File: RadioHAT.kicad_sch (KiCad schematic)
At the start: 2 parts, among them J1 RPi_GPIO

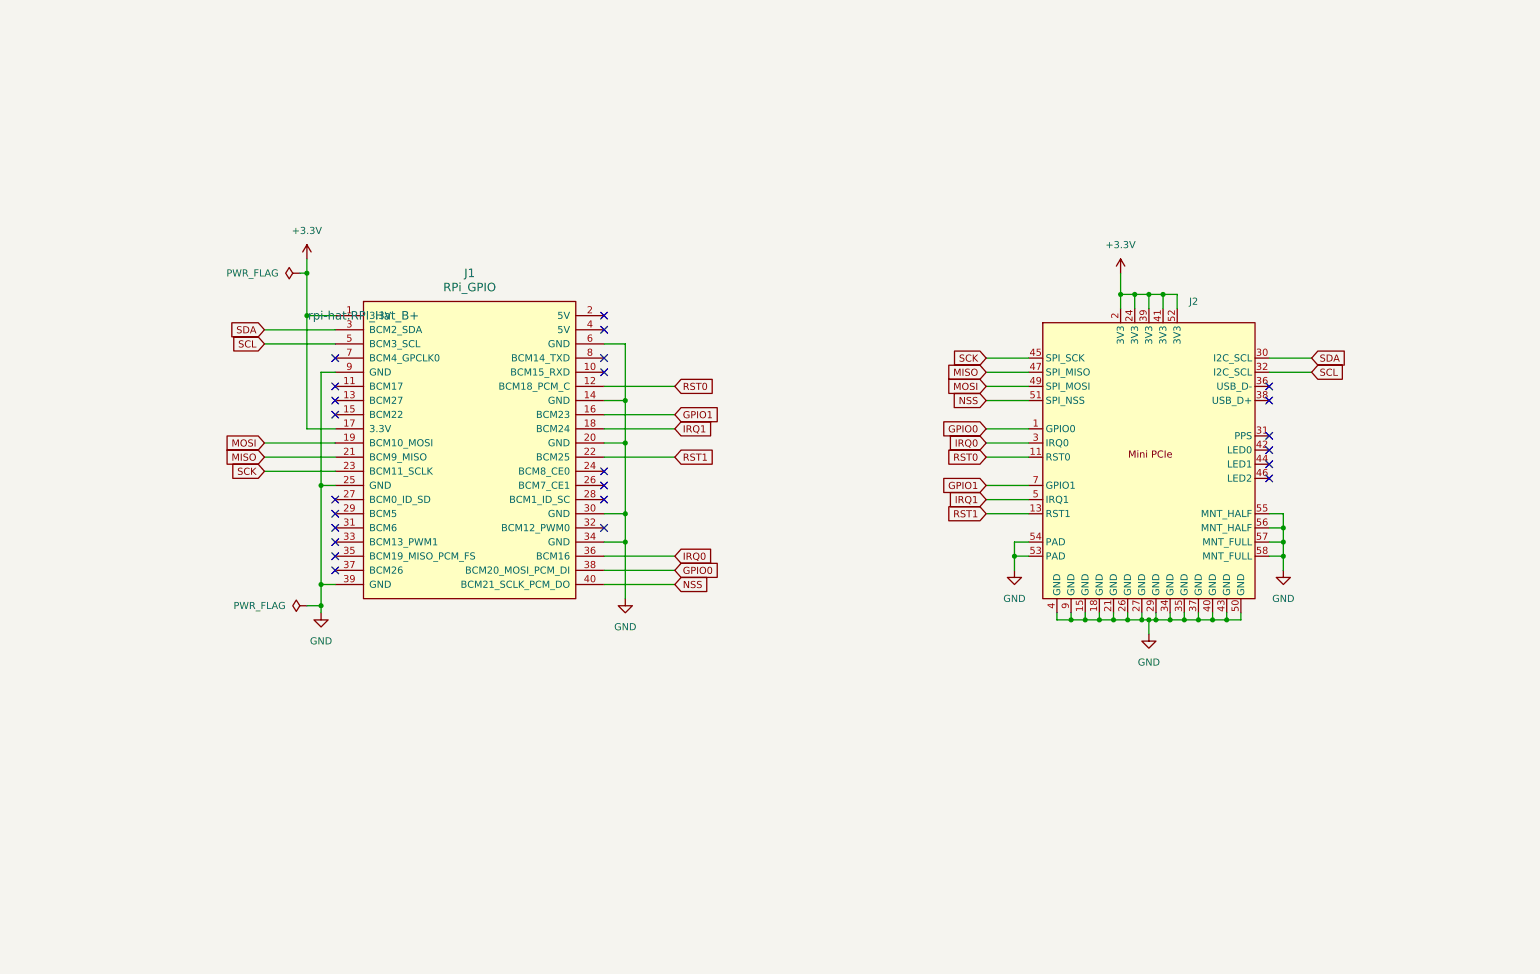
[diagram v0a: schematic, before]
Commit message: HAT rev C (GPIO sense, current measure, LDO)
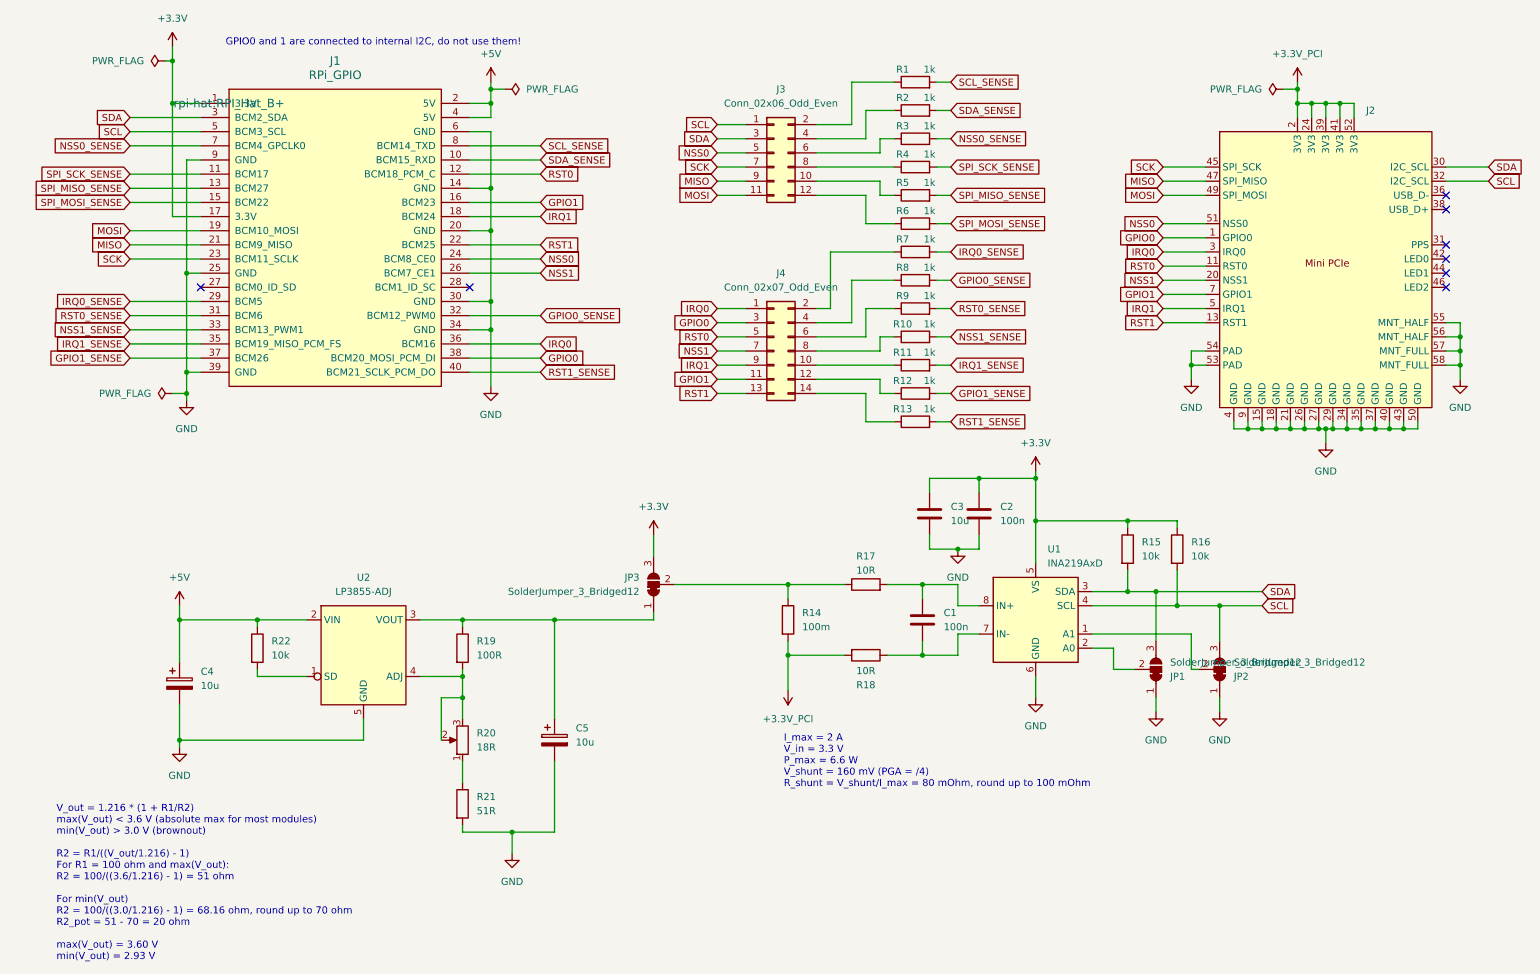
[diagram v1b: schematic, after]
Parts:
- added C1, C2: 100n, Capacitor_SMD:C_0603_1608Metric_Pad1.08x0.95mm_HandSolder, symbol Device:C
- added C3: 10u, Capacitor_SMD:C_0603_1608Metric_Pad1.08x0.95mm_HandSolder, symbol Device:C
- added C4, C5: 10u, Capacitor_Tantalum_SMD:CP_EIA-3216-18_Kemet-A, symbol Device:C_Polarized
- added J3: Conn_02x06_Odd_Even, Connector_PinHeader_2.54mm:PinHeader_2x06_P2.54mm_Vertical, symbol Connector_Generic:Conn_02x06_Odd_Even
- added J4: Conn_02x07_Odd_Even, Connector_PinHeader_2.54mm:PinHeader_2x07_P2.54mm_Vertical, symbol Connector_Generic:Conn_02x07_Odd_Even
- added JP1, JP2, JP3: SolderJumper_3_Bridged12, Jumper:SolderJumper-3_P1.3mm_Bridged12_Pad1.0x1.5mm_NumberLabels, symbol Jumper:SolderJumper_3_Bridged12
- added R1, R10, R11, R12, R13, R2, R3, R4, R5, R6, R7, R8, R9: 1k, Resistor_SMD:R_0805_2012Metric_Pad1.20x1.40mm_HandSolder, symbol Device:R
- added R14: 100m, Resistor_SMD:R_2816_7142Metric_Pad3.20x4.45mm_HandSolder, symbol Device:R
- added R15, R16, R22: 10k, Resistor_SMD:R_0603_1608Metric_Pad0.98x0.95mm_HandSolder, symbol Device:R
- added R17, R18: 10R, Resistor_SMD:R_0603_1608Metric_Pad0.98x0.95mm_HandSolder, symbol Device:R
- added R19: 100R, Resistor_SMD:R_0603_1608Metric_Pad0.98x0.95mm_HandSolder, symbol Device:R
- added R20: 18R, RadioHAT:3362P1200LF, symbol Device:R_Potentiometer
- added R21: 51R, Resistor_SMD:R_0603_1608Metric_Pad0.98x0.95mm_HandSolder, symbol Device:R
- added U1: INA219AxD, Package_SO:SOIC-8_3.9x4.9mm_P1.27mm, symbol Sensor_Energy:INA219AxD
- added U2: LP3855-ADJ, RadioHAT:SOT150P700X180-5N, symbol RadioHAT:LP3855-ADJ
- J2: footprint RadioHAT:Mini_PCIe -> RadioHAT:Mini_PCIe_Latch
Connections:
- net +3.3V: now also C2.1, C3.1, JP3.3 (B), R15.1, R16.1, U1.5 (VS); no longer J2.2 (3V3), J2.24 (3V3), J2.39 (3V3), J2.41 (3V3), J2.52 (3V3)
- net GND: now also C2.2, C3.2, C4.2, C5.2, JP1.1 (A), JP2.1 (A), R21.2, U1.6 (GND), U2.5 (GND)
- net GPIO0: now also J4.3 (Pin_3)
- net GPIO1: now also J4.11 (Pin_11)
- net IRQ0: now also J4.1 (Pin_1)
- net IRQ1: now also J4.9 (Pin_9)
- net MISO: now also J3.9 (Pin_9)
- net MOSI: now also J3.11 (Pin_11)
- net RST0: now also J4.5 (Pin_5)
- net RST1: now also J4.13 (Pin_13)
- net SCK: now also J3.7 (Pin_7)
- net SCL: now also J3.1 (Pin_1), JP2.3 (B), R16.2, U1.4 (SCL)
- net SDA: now also J3.3 (Pin_3), JP1.3 (B), R15.2, U1.3 (SDA)
- net SDA_SENSE: now reaches J1.10 (BCM15_RXD)
- net SDA_SENSE: now also R2.2
- net SPI_SCK_SENSE: now reaches J1.11 (BCM17)
- net SPI_SCK_SENSE: now also R4.2
- net SPI_MISO_SENSE: now reaches J1.13 (BCM27)
- net SPI_MISO_SENSE: now also R5.2
- net SPI_MOSI_SENSE: now reaches J1.15 (BCM22)
- net SPI_MOSI_SENSE: now also R6.2
- net +5V: now reaches J1.2 (5V)
- net +5V: now also J1.4 (5V), C4.1, R22.1, U2.2 (VIN)
- net NSS0: now reaches J1.24 (BCM8_CE0)
- net NSS0: now also J2.51 (NSS0), J3.5 (Pin_5)
- net NSS1: now reaches J1.26 (BCM7_CE1)
- net NSS1: now also J2.20 (NSS1), J4.7 (Pin_7)
- net IRQ0_SENSE: now reaches J1.29 (BCM5)
- net IRQ0_SENSE: now also R7.2
- net RST0_SENSE: now reaches J1.31 (BCM6)
- net RST0_SENSE: now also R9.2
- net GPIO0_SENSE: now reaches J1.32 (BCM12_PWM0)
- net GPIO0_SENSE: now also R8.2
- net NSS1_SENSE: now reaches J1.33 (BCM13_PWM1)
- net NSS1_SENSE: now also R10.2
- net IRQ1_SENSE: now reaches J1.35 (BCM19_MISO_PCM_FS)
- net IRQ1_SENSE: now also R11.2
- net GPIO1_SENSE: now reaches J1.37 (BCM26)
- net GPIO1_SENSE: now also R12.2
- net NSS0_SENSE: now reaches J1.7 (BCM4_GPCLK0)
- net NSS0_SENSE: now also R3.2
- net SCL_SENSE: now reaches J1.8 (BCM14_TXD)
- net SCL_SENSE: now also R1.2
- net NSS renamed RST1_SENSE
- net RST1_SENSE: now also R13.2; no longer J2.51 (SPI_NSS)
- new net: JP1.2 (C), U1.2 (A0)
- new net: J4.12 (Pin_12), R12.1
- new net: JP2.2 (C), U1.1 (A1)
- new net: JP3.2 (C), R14.1, R17.1
- new net: C1.1, R17.2, U1.8 (IN+)
- new net: J3.2 (Pin_2), R1.1
- new net: C1.2, R18.1, U1.7 (IN-)
- new net: J3.4 (Pin_4), R2.1
- new net: R22.2, U2.1 (SD)
- new net: C5.1, JP3.1 (A), R19.1, U2.3 (VOUT)
- new net: R19.2, R20.2, R20.3, U2.4 (ADJ)
- new net: J4.10 (Pin_10), R11.1
- new net: J3.10 (Pin_10), R5.1
- new net: J3.12 (Pin_12), R6.1
- new net: J4.14 (Pin_14), R13.1
- new net: J4.2 (Pin_2), R7.1
- new net: J4.4 (Pin_4), R8.1
- new net: J4.6 (Pin_6), R9.1
- new net: J4.8 (Pin_8), R10.1
- new net: R20.1, R21.1
- new net: J3.6 (Pin_6), R3.1
- new net: J3.8 (Pin_8), R4.1
- new net +3.3V_PCI: J2.2 (3V3), J2.24 (3V3), J2.39 (3V3), J2.41 (3V3), J2.52 (3V3), R14.2, R18.2
- no-connect marks 24 -> 8
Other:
- note added: "GPIO0 and 1 are connected to internal I2C, do not use them!"
- note added: "I_max = 2 A V_in = 3.3 V P_max = 6.6 W V_shunt = 160 mV (PGA = /4) R_shunt = V_shunt/I_max = 80 mOhm, round up to 100 mOhm"
- note added: "V_out = 1.216 * (1 + R1/R2) max(V_out) < 3.6 V (absolute max for most modules) min(V_out) > 3.0 V (brownout) R2 = R1/((V_out/1.216) - 1) For R1 = 100 ohm and max(V_out): R2 = 100/((3.6/1.216) - 1) = 51 ohm For min(V_out) R2 = 100/((3.0/1.216) - 1) = 68.16 ohm, round up to 70 ohm R2_pot = 51 - 70 = 20 ohm max(V_out) = 3.60 V min(V_out) = 2.93 V"
- moved on the sheet: J1

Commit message: Update to use new RPi HAT
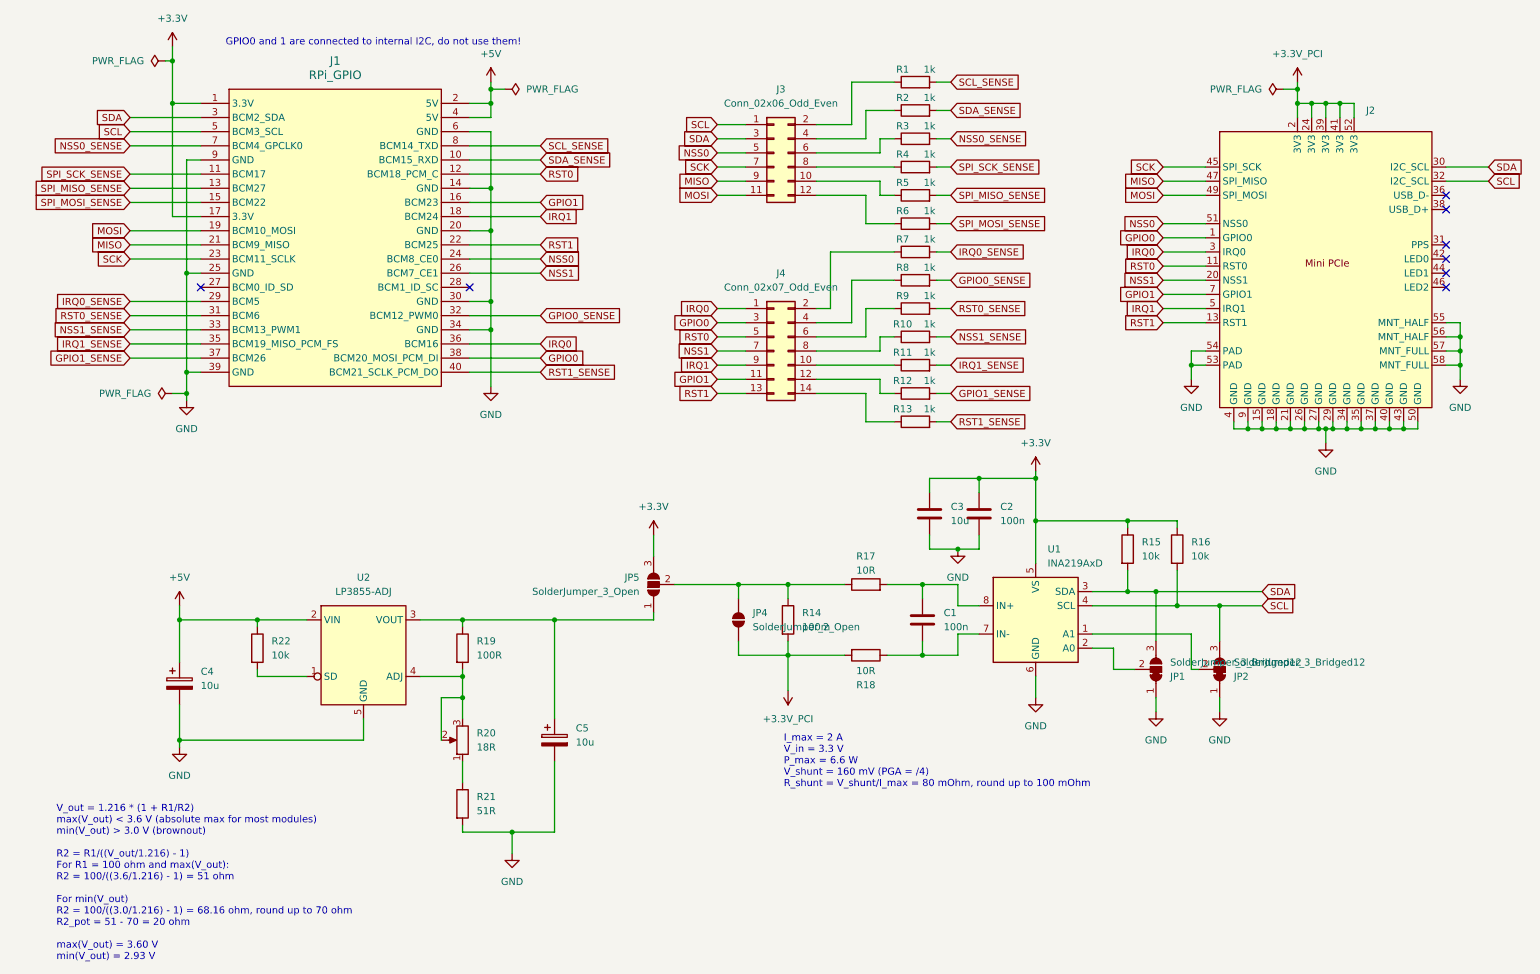
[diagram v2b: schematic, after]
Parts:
- removed JP3: SolderJumper_3_Bridged12, Jumper:SolderJumper-3_P1.3mm_Bridged12_Pad1.0x1.5mm_NumberLabels, symbol Jumper:SolderJumper_3_Bridged12
- added JP4: SolderJumper_2_Open, Jumper:SolderJumper-2_P1.3mm_Open_Pad1.0x1.5mm, symbol Jumper:SolderJumper_2_Open
- added JP5: SolderJumper_3_Open, Jumper:SolderJumper-3_P1.3mm_Open_Pad1.0x1.5mm_NumberLabels, symbol Jumper:SolderJumper_3_Open
- J1: footprint rpi-hat:RPI_Hat_B+ -> RadioHAT:RPI_Hat_B+; symbol rpi-hat:RPi_GPIO -> RadioHAT:RPi_GPIO
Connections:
- net +3.3V: now also JP5.3 (B)
- net +3.3V_PCI: now also JP4.1 (A)
- net at R14.1, R17.1: now also JP4.2 (B), JP5.2 (C)
- net at C5.1, R19.1, U2.3 (VOUT): now also JP5.1 (A)
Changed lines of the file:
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@@
 	)
 	(junction
+		(at 140.97 123.19)
+		(diameter 0)
+		(color 0 0 0 0)
+	)
+	(junction
 		(at 210.82 124.46)
 		(diameter 0)
@@
 	(wire
 		(pts
+			(xy 140.97 135.89) (xy 149.86 135.89)
+		)
+		(stroke
+			(width 0)
+			(type default)
+		)
+	)
+	(wire
+		(pts
 			(xy 137.16 50.8) (xy 142.24 50.8)
 		)
@@
 	(wire
 		(pts
+			(xy 140.97 123.19) (xy 140.97 125.73)
+		)
+		(stroke
+			(width 0)
+			(type default)
+		)
+	)
+	(wire
+		(pts
 			(xy 217.17 58.42) (xy 224.79 58.42)
 		)
@@
 	(wire
 		(pts
+			(xy 140.97 123.19) (xy 149.86 123.19)
+		)
+		(stroke
+			(width 0)
+			(type default)
+		)
+	)
+	(wire
+		(pts
 			(xy 270.51 83.82) (xy 270.51 86.36)
 		)
@@
 	(wire
 		(pts
-			(xy 129.54 123.19) (xy 149.86 123.19)
+			(xy 129.54 123.19) (xy 140.97 123.19)
 		)
 		(stroke
@@
 	(wire
 		(pts
+			(xy 140.97 133.35) (xy 140.97 135.89)
+		)
+		(stroke
+			(width 0)
+			(type default)
+		)
+	)
+	(wire
+		(pts
 			(xy 245.11 95.25) (xy 246.38 95.25)
 		)
@@
 	)
 	(symbol
+		(lib_id "Jumper:SolderJumper_2_Open")
+		(at 140.97 129.54 90)
+		(unit 1)
+		(exclude_from_sim no)
+		(in_bom no)
+		(on_board yes)
+		(dnp no)
+		(fields_autoplaced yes)
+		(property "Reference" "JP4"
+			(at 143.51 128.2699 90)
+			(effects
+				(font
+					(size 1.27 1.27)
+				)
+				(justify right)
+			)
+		)
+		(property "Value" "SolderJumper_2_Open"
+			(at 143.51 130.8099 90)
+			(effects
+				(font
+					(size 1.27 1.27)
+				)
+				(justify right)
+			)
+		)
+		(property "Footprint" "Jumper:SolderJumper-2_P1.3mm_Open_Pad1.0x1.5mm"
+			(at 140.97 129.54 0)
+			(effects
+				(font
+					(size 1.27 1.27)
+				)
+				(hide yes)
+			)
+		)
+		(property "Datasheet" "~"
+			(at 140.97 129.54 0)
+			(effects
+				(font
+					(size 1.27 1.27)
+				)
+				(hide yes)
+			)
+		)
+		(property "Description" "Solder Jumper, 2-pole, open"
+			(at 140.97 129.54 0)
+			(effects
+				(font
+					(size 1.27 1.27)
+				)
+				(hide yes)
+			)
+		)
+		(pin "1"
+		)
+		(pin "2"
+		)
+		(instances
+			(project ""
+				(path "/b81b30b5-0f95-4689-93f2-268be91e8e59"
+					(reference "JP4")
+					(unit 1)
+				)
+			)
+		)
+	)
+	(symbol
 		(lib_id "power:GND")
 		(at 41.91 90.17 0)
@@
 	)
 	(symbol
+		(lib_id "Jumper:SolderJumper_3_Open")
+		(at 125.73 123.19 90)
+		(unit 1)
+		(exclude_from_sim no)
+		(in_bom no)
+		(on_board yes)
+		(dnp no)
+		(property "Reference" "JP5"
+			(at 123.19 121.9199 90)
+			(effects
+				(font
+					(size 1.27 1.27)
+				)
+				(justify left)
+			)
+		)
+		(property "Value" "SolderJumper_3_Open"
+			(at 123.19 124.4599 90)
+			(effects
+				(font
+					(size 1.27 1.27)
+				)
+				(justify left)
+			)
+		)
+		(property "Footprint" "Jumper:SolderJumper-3_P1.3mm_Open_Pad1.0x1.5mm_NumberLabels"
+			(at 125.73 123.19 0)
+			(effects
+				(font
+					(size 1.27 1.27)
+				)
+				(hide yes)
+			)
+		)
+		(property "Datasheet" "~"
+			(at 125.73 123.19 0)
+			(effects
+				(font
+					(size 1.27 1.27)
+				)
+				(hide yes)
+			)
+		)
+		(property "Description" "Solder Jumper, 3-pole, open"
+			(at 125.73 123.19 0)
+			(effects
+				(font
+					(size 1.27 1.27)
+				)
+				(hide yes)
+			)
+		)
+		(pin "1"
+		)
+		(pin "3"
+		)
+		(pin "2"
+		)
+		(instances
+			(project ""
+				(path "/b81b30b5-0f95-4689-93f2-268be91e8e59"
+					(reference "JP5")
+					(unit 1)
+				)
+			)
+		)
+	)
+	(symbol
 		(lib_id "Device:R")
 		(at 172.72 33.02 90)
@@
 	)
 	(symbol
-		(lib_id "Jumper:SolderJumper_3_Bridged12")
-		(at 125.73 123.19 90)
-		(unit 1)
-		(exclude_from_sim no)
-		(in_bom no)
-		(on_board yes)
-		(dnp no)
-		(fields_autoplaced yes)
-		(property "Reference" "JP3"
-			(at 123.19 121.9199 90)
-			(effects
-				(font
-					(size 1.27 1.27)
-				)
-				(justify left)
-			)
-		)
-		(property "Value" "SolderJumper_3_Bridged12"
-			(at 123.19 124.4599 90)
-			(effects
-				(font
-					(size 1.27 1.27)
-				)
-				(justify left)
-			)
-		)
-		(property "Footprint" "Jumper:SolderJumper-3_P1.3mm_Bridged12_Pad1.0x1.5mm_NumberLabels"
-			(at 125.73 123.19 0)
-			(effects
-				(font
-					(size 1.27 1.27)
-				)
-				(hide yes)
-			)
-		)
-		(property "Datasheet" "~"
-			(at 125.73 123.19 0)
-			(effects
-				(font
-					(size 1.27 1.27)
-				)
-				(hide yes)
-			)
-		)
-		(property "Description" "3-pole Solder Jumper, pins 1+2 closed/bridged"
-			(at 125.73 123.19 0)
-			(effects
-				(font
-					(size 1.27 1.27)
-				)
-				(hide yes)
-			)
-		)
-		(pin "1"
-		)
-		(pin "3"
-		)
-		(pin "2"
-		)
-		(instances
-			(project ""
-				(path "/b81b30b5-0f95-4689-93f2-268be91e8e59"
-					(reference "JP3")
-					(unit 1)
-				)
-			)
-		)
-	)
-	(symbol
 		(lib_id "power:+3.3V")
 		(at 241.3 33.02 0)
@@
 	)
 	(symbol
-		(lib_id "rpi-hat:RPi_GPIO")
-		(at 49.53 36.83 0)
+		(lib_id "RadioHAT:RPi_GPIO")
+		(at 67.31 31.75 0)
 		(unit 1)
 		(exclude_from_sim no)
@@
 			)
 		)
-		(property "Footprint" "rpi-hat:RPI_Hat_B+"
-			(at 49.53 36.83 0)
+		(property "Footprint" "RadioHAT:RPI_Hat_B+"
+			(at 67.31 31.75 0)
 			(effects
 				(font
-					(size 1.524 1.524)
+					(size 1.27 1.27)
 				)
+				(hide yes)
 			)
 		)
 		(property "Datasheet" ""
-			(at 49.53 36.83 0)
+			(at 67.31 31.75 0)
 			(effects
 				(font
-					(size 1.524 1.524)
+					(size 1.27 1.27)
 				)
+				(hide yes)
 			)
 		)
 		(property "Description" ""
-			(at 49.53 36.83 0)
+			(at 67.31 31.75 0)
 			(effects
 				(font
